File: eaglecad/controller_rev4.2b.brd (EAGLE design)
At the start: 40 x 29.5 mm, 79 parts, among them U100 STM32L452XX_QFPN48, U101 TCAN330, U200 TPS63070, U300 STSPIN230, U301 TSV991ILT, U302 AS5047P, U400 STSPIN250, U401 TSV991ILT, X101 ABM10-16MHz

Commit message: minor changes
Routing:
- net SENSE_BLDC: track 19.3 -> 16.6 mm
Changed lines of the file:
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@@
 <drawing>
 <settings>
-<setting alwaysvectorfont="yes"/>
+<setting alwaysvectorfont="no"/>
 <setting verticaltext="up"/>
 </settings>
@@
 <wire x1="11" y1="20.4" x2="10.31" y2="20.4" width="0.254" layer="1"/>
 <via x="10.31" y="20.4" extent="1-16" drill="0.254"/>
-<wire x1="10.31" y1="20.4" x2="9.46" y2="20.4" width="0.254" layer="16"/>
-<wire x1="9.46" y1="20.4" x2="8.53" y2="21.33" width="0.254" layer="16"/>
-<wire x1="8.53" y1="21.33" x2="8.53" y2="22.62" width="0.254" layer="16"/>
-<wire x1="8.53" y1="22.62" x2="9.06" y2="23.15" width="0.254" layer="16"/>
-<wire x1="9.06" y1="23.15" x2="10.32" y2="23.15" width="0.254" layer="16"/>
 <via x="10.32" y="23.15" extent="1-16" drill="0.254"/>
 <wire x1="10.97" y1="23.15" x2="11" y2="23.18" width="0.254" layer="1"/>
@@
 <wire x1="13.37" y1="27.92" x2="15.37" y2="27.92" width="0.45" layer="1"/>
 <wire x1="15.37" y1="27.92" x2="18.45" y2="27.92" width="0.254" layer="1"/>
+<wire x1="10.32" y1="23.15" x2="10.32" y2="20.41" width="0.254" layer="16"/>
+<wire x1="10.32" y1="20.41" x2="10.31" y2="20.4" width="0.254" layer="16"/>
 </signal>
 <signal name="W">
@@
 <wire x1="22.34" y1="17.17" x2="21.34" y2="17.17" width="0.25" layer="1"/>
 <wire x1="13.17" y1="21.01" x2="13.14" y2="21.04" width="0.254" layer="1"/>
-<via x="18.83" y="17.2574" extent="1-16" drill="0.254"/>
-<wire x1="18.83" y1="17.2574" x2="18.83" y2="17.26" width="0.254" layer="16"/>
-<wire x1="18.83" y1="17.26" x2="15.08" y2="21.01" width="0.254" layer="16"/>
-<via x="15.08" y="21.01" extent="1-16" drill="0.254"/>
-<wire x1="18.83" y1="17.2474" x2="18.83" y2="17.2574" width="0.254" layer="1"/>
-<wire x1="15.08" y1="21.01" x2="13.17" y2="21.01" width="0.254" layer="1"/>
 <wire x1="24.625" y1="17.25" x2="22.42" y2="17.25" width="0.254" layer="1"/>
 <wire x1="22.42" y1="17.25" x2="22.34" y2="17.17" width="0.254" layer="1"/>
 <wire x1="21.34" y1="17.17" x2="21.2626" y2="17.2474" width="0.254" layer="1"/>
-<wire x1="21.2626" y1="17.2474" x2="18.83" y2="17.2474" width="0.254" layer="1"/>
+<wire x1="21.34" y1="17.17" x2="18.23" y2="17.17" width="0.254" layer="1"/>
+<wire x1="18.23" y1="17.17" x2="16.1" y2="19.3" width="0.254" layer="1"/>
+<via x="16.1" y="19.3" extent="1-16" drill="0.254"/>
+<wire x1="16.1" y1="19.3" x2="14.35" y2="21.05" width="0.254" layer="16"/>
+<via x="14.35" y="21.05" extent="1-16" drill="0.254"/>
+<wire x1="14.35" y1="21.05" x2="14.34" y2="21.04" width="0.254" layer="1"/>
+<wire x1="14.34" y1="21.04" x2="13.14" y2="21.04" width="0.254" layer="1"/>
 </signal>
 <signal name="BLDC_INUL">
@@
 <wire x1="18.4735875" y1="9.3474" x2="17.3" y2="8.1738125" width="0.254" layer="1"/>
 <wire x1="17.3" y1="8.1738125" x2="17.3" y2="7.3" width="0.254" layer="1"/>
-<wire x1="17.3" y1="7.3" x2="17.3" y2="3.3" width="0.254" layer="1"/>
+<wire x1="17.3" y1="7.3" x2="17.3" y2="5.4" width="0.254" layer="1"/>
+<wire x1="17.3" y1="5.4" x2="17.3" y2="3.3" width="0.254" layer="1"/>
+<wire x1="17.3" y1="5.4" x2="17.3" y2="5.4" width="0.254" layer="1"/>
 </signal>
 <signal name="ADDR_0">

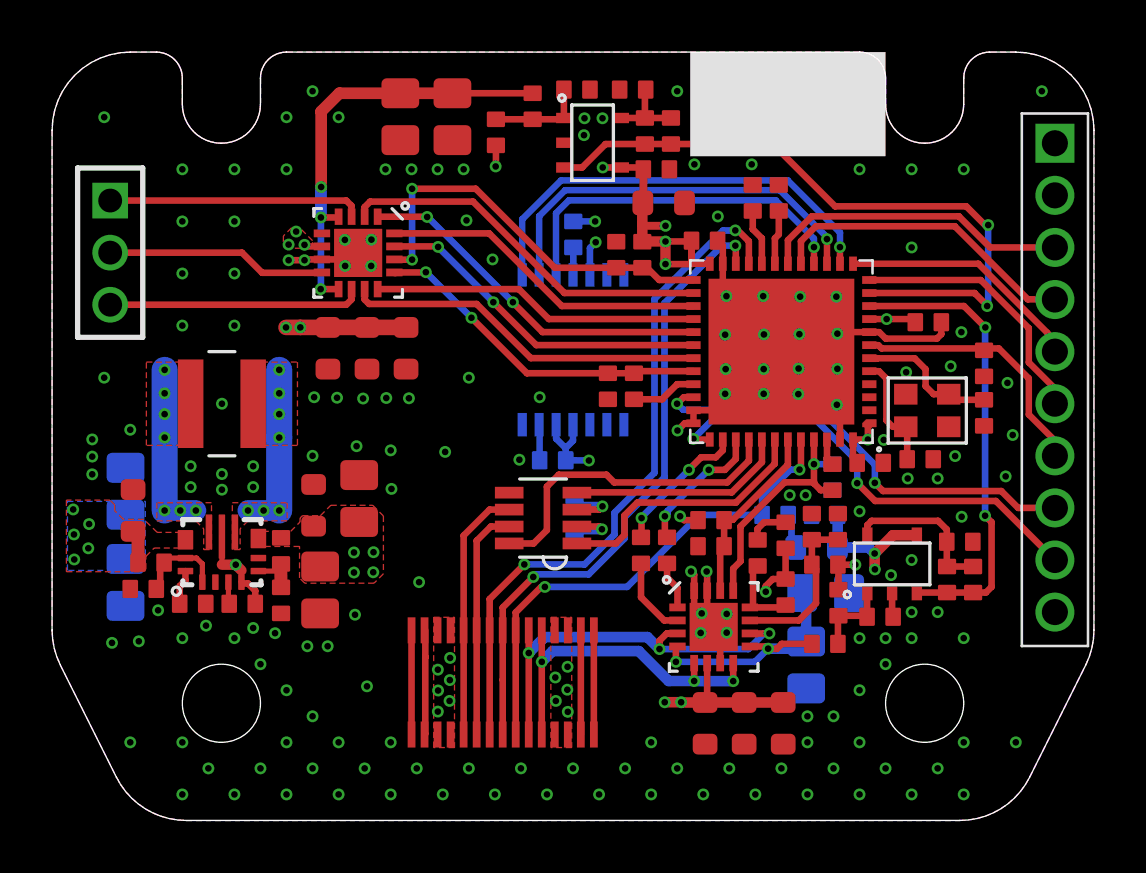
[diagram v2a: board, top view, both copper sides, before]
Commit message: Final polish on v4.2b; sent off to OSH Park.
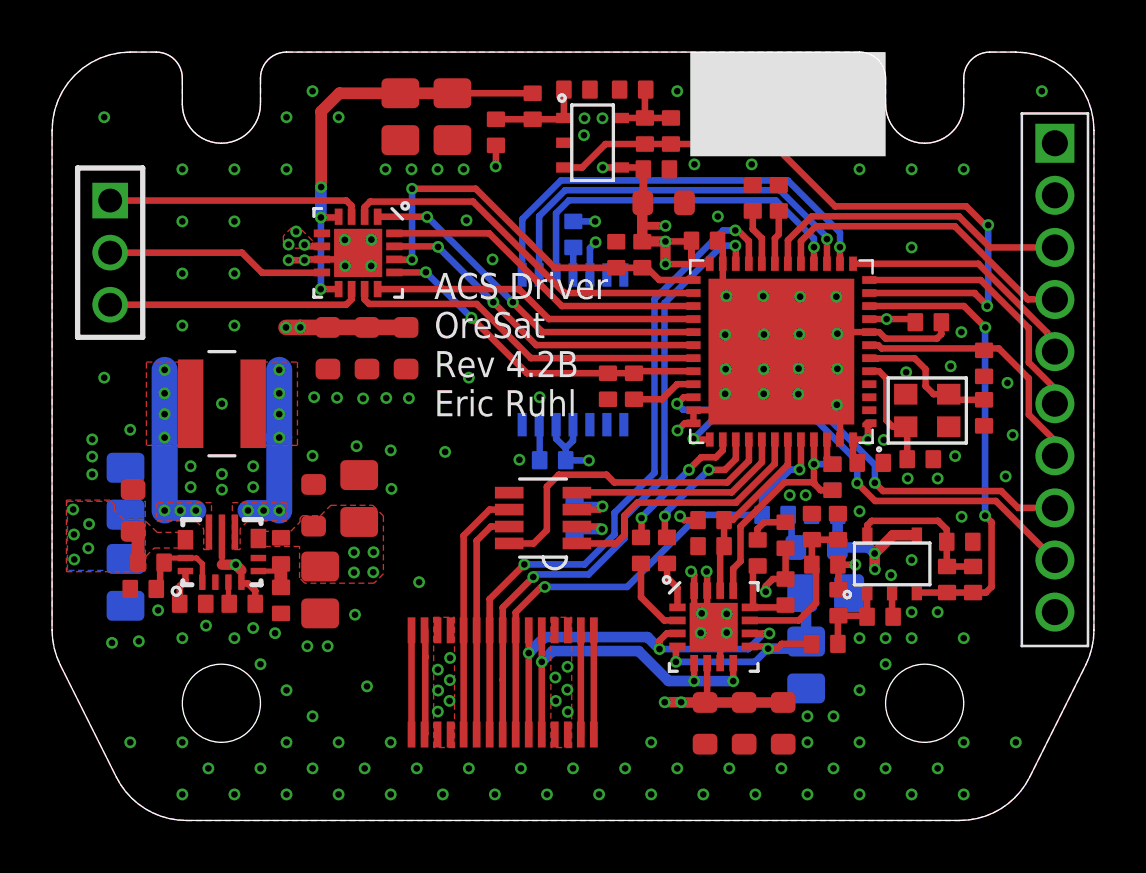
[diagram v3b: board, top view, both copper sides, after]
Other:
- board text added: "ACS Driver OreSat Rev 4.2B Eric Ruhl"
- board text removed: "ACS Driver OreSat Rev 4.2 Eric Ruhl"
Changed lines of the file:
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@@
 <?xml version="1.0" encoding="utf-8"?>
 <!DOCTYPE eagle SYSTEM "eagle.dtd">
-<eagle version="9.3.0">
+<eagle version="9.5.1">
 <drawing>
 <settings>
@@
 <setting verticaltext="up"/>
 </settings>
-<grid distance="1" unitdist="mm" unit="mm" style="lines" multiple="1" display="yes" altdistance="0.01" altunitdist="mm" altunit="mm"/>
+<grid distance="0.5" unitdist="mm" unit="mm" style="lines" multiple="1" display="yes" altdistance="0.01" altunitdist="mm" altunit="mm"/>
 <layers>
 <layer number="1" name="Top" color="59" fill="1" visible="yes" active="yes"/>
-<layer number="2" name="Route2" color="58" fill="1" visible="yes" active="yes"/>
+<layer number="2" name="Route2" color="58" fill="1" visible="no" active="yes"/>
 <layer number="3" name="Route3" color="4" fill="3" visible="no" active="no"/>
 <layer number="4" name="Route4" color="1" fill="4" visible="no" active="no"/>
@@
 <layer number="13" name="Route13" color="4" fill="5" visible="no" active="no"/>
 <layer number="14" name="Route14" color="1" fill="6" visible="no" active="no"/>
-<layer number="15" name="Route15" color="16" fill="1" visible="yes" active="yes"/>
-<layer number="16" name="Bottom" color="38" fill="1" visible="yes" active="yes"/>
+<layer number="15" name="Route15" color="16" fill="1" visible="no" active="yes"/>
+<layer number="16" name="Bottom" color="38" fill="1" visible="no" active="yes"/>
 <layer number="17" name="Pads" color="2" fill="1" visible="yes" active="yes"/>
 <layer number="18" name="Vias" color="2" fill="1" visible="yes" active="yes"/>
@@
 <layer number="20" name="Dimension" color="24" fill="1" visible="yes" active="yes"/>
 <layer number="21" name="tPlace" color="7" fill="1" visible="yes" active="yes"/>
-<layer number="22" name="bPlace" color="7" fill="1" visible="yes" active="yes"/>
+<layer number="22" name="bPlace" color="7" fill="1" visible="no" active="yes"/>
 <layer number="23" name="tOrigins" color="15" fill="1" visible="yes" active="yes"/>
-<layer number="24" name="bOrigins" color="15" fill="1" visible="yes" active="yes"/>
-<layer number="25" name="tNames" color="7" fill="1" visible="yes" active="yes"/>
-<layer number="26" name="bNames" color="7" fill="1" visible="yes" active="yes"/>
+<layer number="24" name="bOrigins" color="15" fill="1" visible="no" active="yes"/>
+<layer number="25" name="tNames" color="7" fill="1" visible="no" active="yes"/>
+<layer number="26" name="bNames" color="7" fill="1" visible="no" active="yes"/>
 <layer number="27" name="tValues" color="7" fill="1" visible="no" active="yes"/>
 <layer number="28" name="bValues" color="7" fill="1" visible="no" active="yes"/>
-<layer number="29" name="tStop" color="7" fill="3" visible="no" active="yes"/>
-<layer number="30" name="bStop" color="7" fill="6" visible="yes" active="yes"/>
+<layer number="29" name="tStop" color="7" fill="3" visible="yes" active="yes"/>
+<layer number="30" name="bStop" color="7" fill="6" visible="no" active="yes"/>
 <layer number="31" name="tCream" color="7" fill="4" visible="no" active="yes"/>
 <layer number="32" name="bCream" color="7" fill="5" visible="no" active="yes"/>
@@
 <layer number="37" name="tTest" color="7" fill="1" visible="no" active="yes"/>
 <layer number="38" name="bTest" color="7" fill="1" visible="no" active="yes"/>
-<layer number="39" name="tKeepout" color="4" fill="11" visible="yes" active="yes"/>
-<layer number="40" name="bKeepout" color="1" fill="11" visible="yes" active="yes"/>
-<layer number="41" name="tRestrict" color="4" fill="10" visible="yes" active="yes"/>
-<layer number="42" name="bRestrict" color="1" fill="10" visible="yes" active="yes"/>
+<layer number="39" name="tKeepout" color="4" fill="11" visible="no" active="yes"/>
+<layer number="40" name="bKeepout" color="1" fill="11" visible="no" active="yes"/>
+<layer number="41" name="tRestrict" color="4" fill="10" visible="no" active="yes"/>
+<layer number="42" name="bRestrict" color="1" fill="10" visible="no" active="yes"/>
 <layer number="43" name="vRestrict" color="2" fill="10" visible="no" active="yes"/>
 <layer number="44" name="Drills" color="7" fill="1" visible="no" active="yes"/>
 <layer number="45" name="Holes" color="7" fill="1" visible="no" active="yes"/>
-<layer number="46" name="Milling" color="3" fill="1" visible="no" active="yes"/>
+<layer number="46" name="Milling" color="3" fill="1" visible="yes" active="yes"/>
 <layer number="47" name="Measures" color="7" fill="1" visible="no" active="yes"/>
 <layer number="48" name="Document" color="7" fill="1" visible="no" active="yes"/>
-<layer number="49" name="Reference" color="7" fill="1" visible="yes" active="yes"/>
+<layer number="49" name="Reference" color="7" fill="1" visible="no" active="yes"/>
 <layer number="50" name="dxf" color="7" fill="1" visible="no" active="no"/>
 <layer number="51" name="tDocu" color="7" fill="1" visible="yes" active="yes"/>
-<layer number="52" name="bDocu" color="7" fill="1" visible="yes" active="yes"/>
+<layer number="52" name="bDocu" color="7" fill="1" visible="no" active="yes"/>
 <layer number="53" name="tGND_GNDA" color="7" fill="1" visible="no" active="no"/>
 <layer number="54" name="bGND_GNDA" color="7" fill="1" visible="no" active="no"/>
@@
 <circle x="33.5" y="4.5" radius="2.5" width="0.1524" layer="39"/>
 <circle x="33.5" y="27.5" radius="2.5" width="0.1524" layer="39"/>
-<text x="17.83" y="8.02" size="1" layer="22" rot="MR0">ACS Driver
+<text x="17.83" y="8.02" size="1" layer="22" font="vector" ratio="10" rot="MR0">ACS Driver
 OreSat
-Rev 4.2
+Rev 4.2B
 Eric Ruhl</text>
 <rectangle x1="24.5" y1="25.5" x2="32" y2="29.5" layer="21"/>
@@
 <rectangle x1="14" y1="20.27" x2="14.26" y2="20.53" layer="29"/>
 <rectangle x1="14" y1="19.7" x2="14.26" y2="19.96" layer="29"/>
+<text x="14.67" y="15.52" size="1" layer="21" font="vector" ratio="10">ACS Driver
+OreSat
+Rev 4.2B
+Eric Ruhl</text>
 </plain>
 <attributes>
@@
 <wire x1="18.3" y1="6.43" x2="18.91" y2="7.04" width="0.4064" layer="16"/>
 <via x="18.3" y="6.43" extent="1-16" drill="0.254"/>
-<wire x1="18.3" y1="6.43" x2="18.3" y2="3.33" width="0.254" layer="1"/>
-<wire x1="18.3" y1="3.33" x2="18.3" y2="3.3" width="0" layer="19" extent="1-1"/>
+<wire x1="18.3" y1="3.3" x2="18.3" y2="6.43" width="0.254" layer="1"/>
 </signal>
 <signal name="OUT2">
@@
 <contactref element="U$2" pad="P$11"/>
 <contactref element="U$2" pad="P$20"/>
-<wire x1="18.8" y1="7.3" x2="18.8" y2="3.3" width="0.254" layer="1"/>
 <wire x1="24.65" y1="5.3542" x2="23.67" y2="5.3542" width="0.4064" layer="16"/>
 <wire x1="23.67" y1="5.3542" x2="22.52" y2="6.5042" width="0.4064" layer="16"/>
@@
 <wire x1="19.2142" y1="6.5042" x2="18.8" y2="6.09" width="0.4064" layer="16"/>
 <via x="18.8" y="6.09" extent="1-16" drill="0.254"/>
-<wire x1="18.8" y1="7.3" x2="19.2142" y2="6.5042" width="0" layer="19" extent="1-16"/>
+<wire x1="18.8" y1="7.3" x2="18.8" y2="6.09" width="0.254" layer="1"/>
+<wire x1="18.8" y1="6.09" x2="18.8" y2="3.3" width="0.254" layer="1"/>
 </signal>
 <signal name="250_REF">
@@
 <contactref element="U300" pad="13"/>
 <wire x1="22.34" y1="17.17" x2="21.34" y2="17.17" width="0.25" layer="1"/>
-<wire x1="13.17" y1="21.01" x2="13.14" y2="21.04" width="0.254" layer="1"/>
 <wire x1="24.625" y1="17.25" x2="22.42" y2="17.25" width="0.254" layer="1"/>
 <wire x1="22.42" y1="17.25" x2="22.34" y2="17.17" width="0.254" layer="1"/>
-<wire x1="21.34" y1="17.17" x2="21.2626" y2="17.2474" width="0.254" layer="1"/>
 <wire x1="21.34" y1="17.17" x2="18.23" y2="17.17" width="0.254" layer="1"/>
 <wire x1="18.23" y1="17.17" x2="16.1" y2="19.3" width="0.254" layer="1"/>
